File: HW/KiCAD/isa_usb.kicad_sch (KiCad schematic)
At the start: 28 parts, among them J1 USB_A, J2 IO ADDR1, J3 IO ADDR2, J4 Conn_01x02_Pin, U1 74LS138, U2 CH375B, U3 74LS139, U4 74LS125, Y1 12M

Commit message: some edit
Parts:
- U2: footprint CH375B:SOP28-LL -> Library:SOP28-LL
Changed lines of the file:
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@@
 			)
 		)
-		(property "Footprint" "CH375B:SOP28-LL"
+		(property "Footprint" "Library:SOP28-LL"
 			(at 140.97 116.84 0)
 			(effects

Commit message: some eidts, remove com
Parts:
- U2: footprint Library:SOP28-LL -> kharon:SOP28-LL
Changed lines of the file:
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@@
 			)
 		)
-		(property "Footprint" "Library:SOP28-LL"
+		(property "Footprint" "kharon:SOP28-LL"
 			(at 140.97 116.84 0)
 			(effects

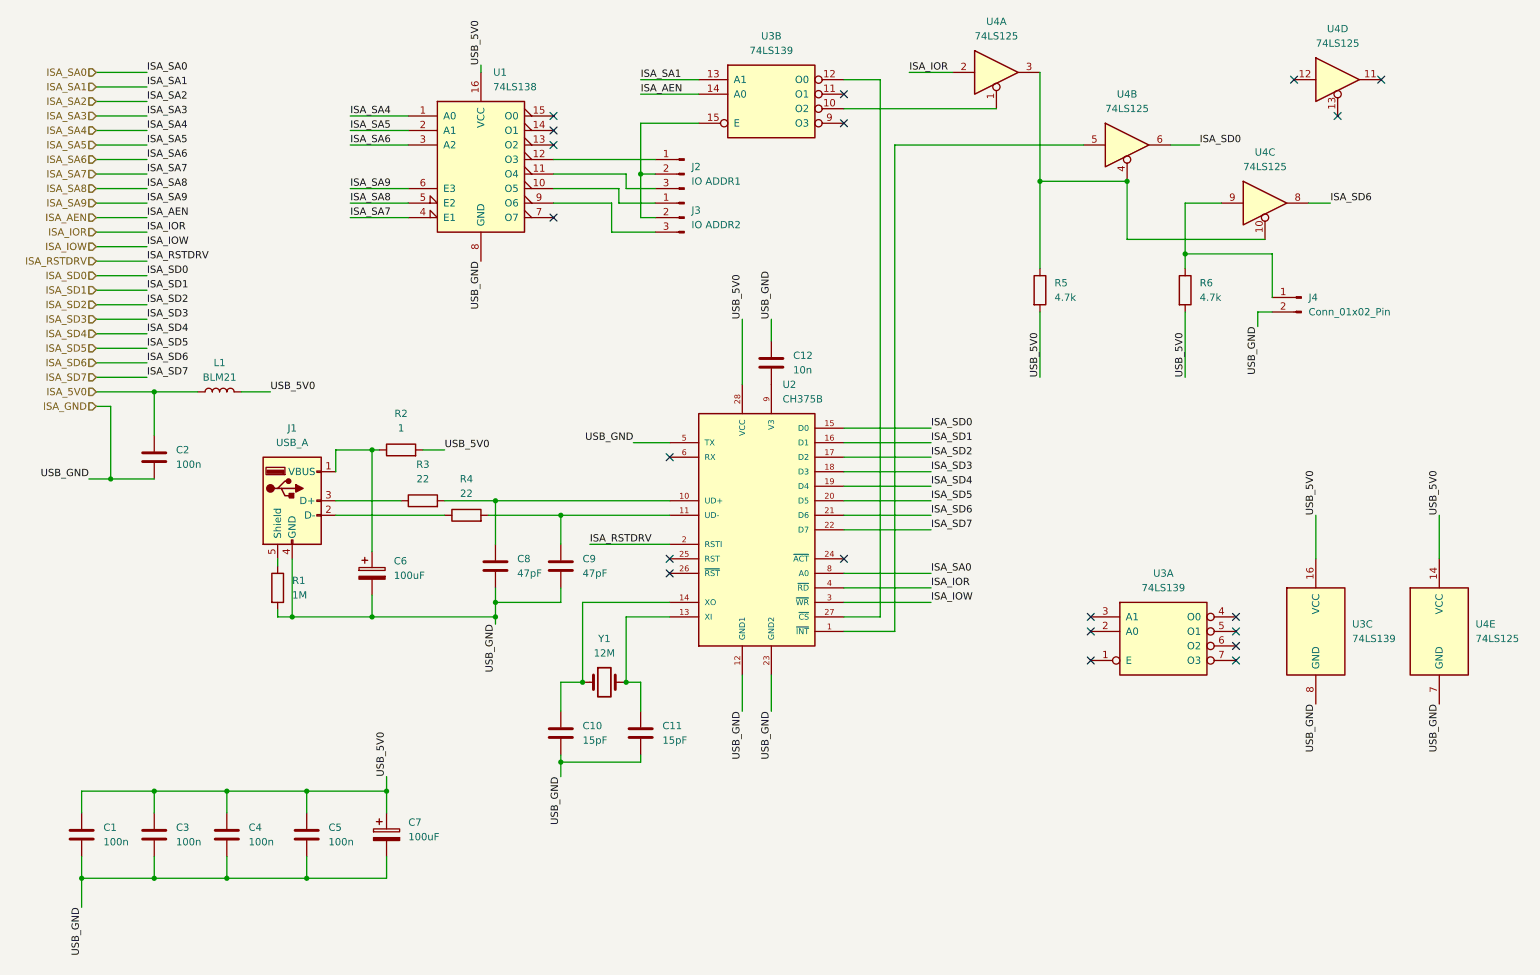
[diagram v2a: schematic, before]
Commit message: some edits, add HP amp
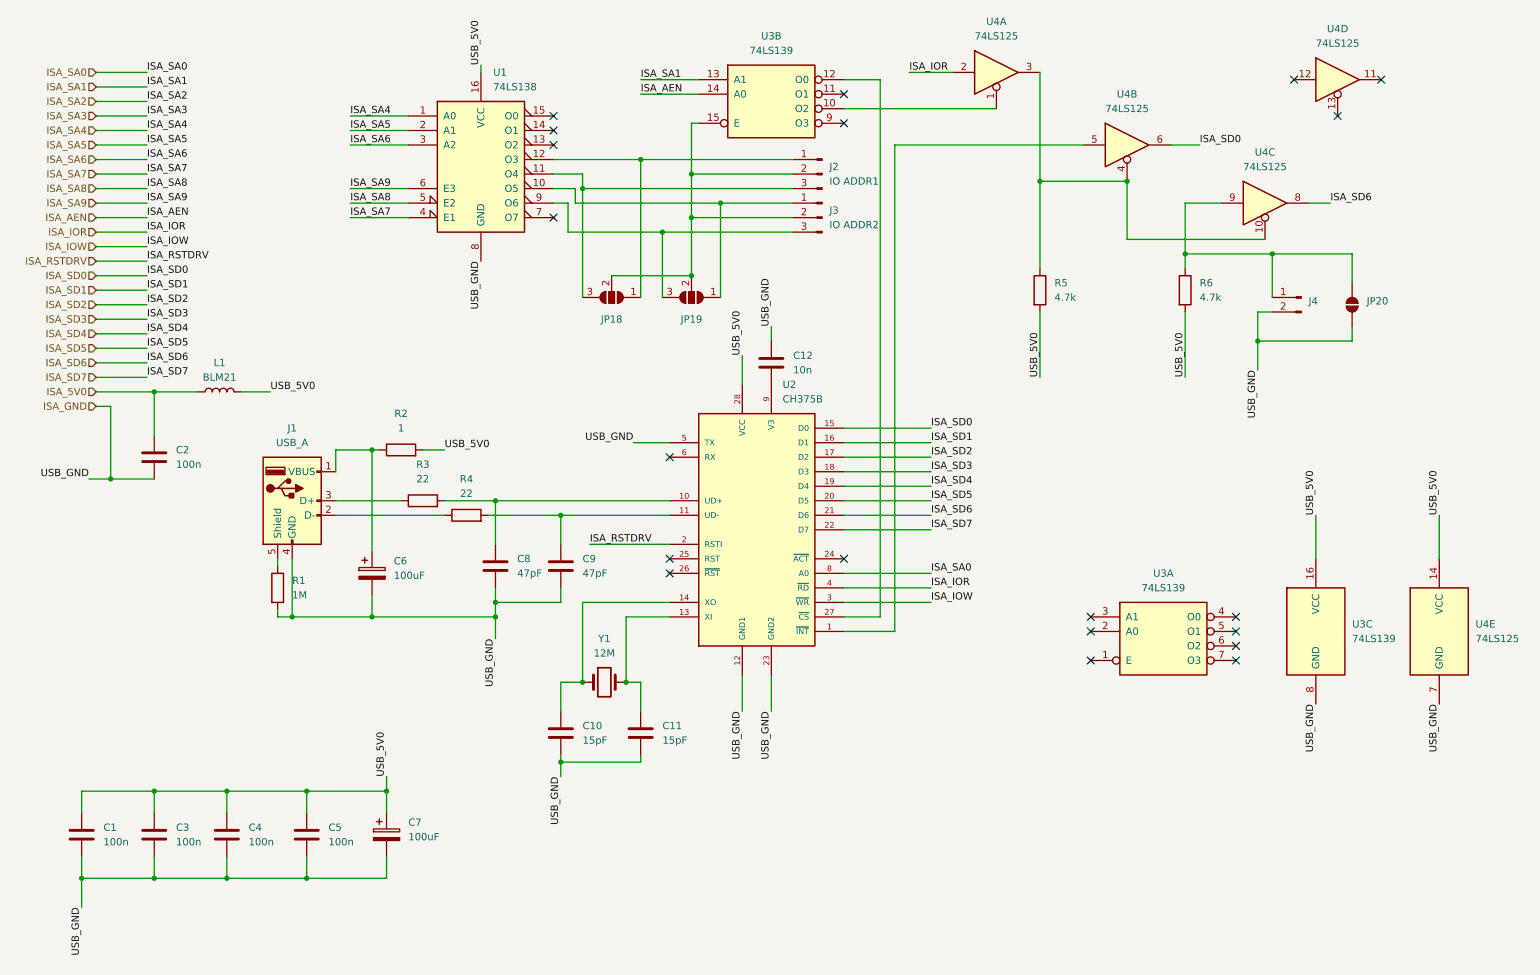
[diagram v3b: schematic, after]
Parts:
- added JP18, JP19: ~, Jumper:SolderJumper-3_P2.0mm_Open_TrianglePad1.0x1.5mm_NumberLabels, symbol Jumper:SolderJumper_3_Open
- added JP20: ~, Jumper:SolderJumper-2_P1.3mm_Open_TrianglePad1.0x1.5mm, symbol Jumper:SolderJumper_2_Open
- J4: value Conn_01x02_Pin -> ~
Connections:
- net ISA_GND: now also JP20.1 (A)
- net at J2.1 (Pin_1), U1.12 (O3): now also JP18.1 (A)
- net at J2.2 (Pin_2), J3.2 (Pin_2), U3.15 (E): now also JP18.2 (C), JP19.2 (C)
- net at J2.3 (Pin_3), U1.11 (O4): now also JP18.3 (B)
- net at J4.1 (Pin_1), R6.1, U4.9: now also JP20.2 (B)
- net at J3.1 (Pin_1), U1.10 (O5): now also JP19.1 (A)
- net at J3.3 (Pin_3), U1.9 (O6): now also JP19.3 (B)
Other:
- moved on the sheet: J2, J3
